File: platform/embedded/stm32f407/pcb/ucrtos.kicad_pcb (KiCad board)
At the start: 2 copper layers, 2 parts, among them J1 nes_gamepad_02x03, J2 STM32F4_Discovery_Header

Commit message: platform stm32f4: pcb: update pcb
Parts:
- moved J1 118.1 mm to (59.7, 120.7), turned to 270 degrees
- moved J2 12.5 mm to (94.4, 78.7)
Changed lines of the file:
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@@
   (general
     (thickness 1.6)
-    (drawings 0)
+    (drawings 2)
     (tracks 0)
     (zones 0)
@@
   )
   (module Connector_IDC:IDC-Header_2x03_P2.54mm_Vertical (layer F.Cu)
-    (at 160.02 58.42)
+    (at 59.69 120.65 270)
     (descr "Through hole straight IDC box header, 2x03, 2.54mm pitch, double rows")
     (tags "Through hole IDC box header THT 2x03 2.54mm double row")
-    (fp_text reference J1 (at 1.27 -6.604) (layer F.SilkS)
+    (fp_text reference J1 (at 1.27 -6.604 270) (layer F.SilkS)
       (effects (font (size 1 1) (thickness 0.15)))
     )
-    (fp_text value nes_gamepad_02x03 (at 1.27 11.684) (layer F.Fab)
+    (fp_text value nes_gamepad_02x03 (at 1.27 11.684 270) (layer F.Fab)
       (effects (font (size 1 1) (thickness 0.15)))
     )
-    (fp_text user %R (at 1.27 2.54) (layer F.Fab)
+    (fp_text user %R (at 1.27 2.54 270) (layer F.Fab)
       (effects (font (size 1 1) (thickness 0.15)))
     )
@@
     (fp_line (start -3.655 -5.6) (end -3.655 -3.06) (layer F.SilkS) (width 0.12))
     (fp_line (start -3.655 -5.6) (end -1.115 -5.6) (layer F.SilkS) (width 0.12))
-    (pad 1 thru_hole rect (at 0 0) (size 1.7272 1.7272) (drill 1.016) (layers *.Cu *.Mask))
-    (pad 2 thru_hole oval (at 2.54 0) (size 1.7272 1.7272) (drill 1.016) (layers *.Cu *.Mask))
-    (pad 3 thru_hole oval (at 0 2.54) (size 1.7272 1.7272) (drill 1.016) (layers *.Cu *.Mask))
-    (pad 4 thru_hole oval (at 2.54 2.54) (size 1.7272 1.7272) (drill 1.016) (layers *.Cu *.Mask))
-    (pad 5 thru_hole oval (at 0 5.08) (size 1.7272 1.7272) (drill 1.016) (layers *.Cu *.Mask))
-    (pad 6 thru_hole oval (at 2.54 5.08) (size 1.7272 1.7272) (drill 1.016) (layers *.Cu *.Mask))
+    (pad 1 thru_hole rect (at 0 0 270) (size 1.7272 1.7272) (drill 1.016) (layers *.Cu *.Mask))
+    (pad 2 thru_hole oval (at 2.54 0 270) (size 1.7272 1.7272) (drill 1.016) (layers *.Cu *.Mask))
+    (pad 3 thru_hole oval (at 0 2.54 270) (size 1.7272 1.7272) (drill 1.016) (layers *.Cu *.Mask))
+    (pad 4 thru_hole oval (at 2.54 2.54 270) (size 1.7272 1.7272) (drill 1.016) (layers *.Cu *.Mask))
+    (pad 5 thru_hole oval (at 0 5.08 270) (size 1.7272 1.7272) (drill 1.016) (layers *.Cu *.Mask))
+    (pad 6 thru_hole oval (at 2.54 5.08 270) (size 1.7272 1.7272) (drill 1.016) (layers *.Cu *.Mask))
     (model ${KISYS3DMOD}/Connector_IDC.3dshapes/IDC-Header_2x03_P2.54mm_Vertical.wrl
       (at (xyz 0 0 0))
@@
   )
   (module w_conn_misc:stm32f4_discovery_header (layer F.Cu)
-    (at 94.410501 66.210501)
+    (at 94.410501 78.74)
     (descr "STM32 F4 Discovery Header")
     (tags "STM32F4 Discovery")
@@
     )
   )
+  (dimension 100.33 (width 0.3) (layer F.SilkS)
+    (gr_text "100.330 mm" (at 95.885 135.45) (layer F.SilkS)
+      (effects (font (size 1.5 1.5) (thickness 0.3)))
+    )
+    (feature1 (pts (xy 146.05 101.6) (xy 146.05 133.936421)))
+    (feature2 (pts (xy 45.72 101.6) (xy 45.72 133.936421)))
+    (crossbar (pts (xy 45.72 133.35) (xy 146.05 133.35)))
+    (arrow1a (pts (xy 146.05 133.35) (xy 144.923496 133.936421)))
+    (arrow1b (pts (xy 146.05 133.35) (xy 144.923496 132.763579)))
+    (arrow2a (pts (xy 45.72 133.35) (xy 46.846504 133.936421)))
+    (arrow2b (pts (xy 45.72 133.35) (xy 46.846504 132.763579)))
+  )
+  (dimension 100.33 (width 0.3) (layer F.SilkS)
+    (gr_text "100.330 mm" (at 32.190001 83.185 270) (layer F.SilkS)
+      (effects (font (size 1.5 1.5) (thickness 0.3)))
+    )
+    (feature1 (pts (xy 39.37 133.35) (xy 33.70358 133.35)))
+    (feature2 (pts (xy 39.37 33.02) (xy 33.70358 33.02)))
+    (crossbar (pts (xy 34.290001 33.02) (xy 34.290001 133.35)))
+    (arrow1a (pts (xy 34.290001 133.35) (xy 33.70358 132.223496)))
+    (arrow1b (pts (xy 34.290001 133.35) (xy 34.876422 132.223496)))
+    (arrow2a (pts (xy 34.290001 33.02) (xy 33.70358 34.146504)))
+    (arrow2b (pts (xy 34.290001 33.02) (xy 34.876422 34.146504)))
+  )
 )

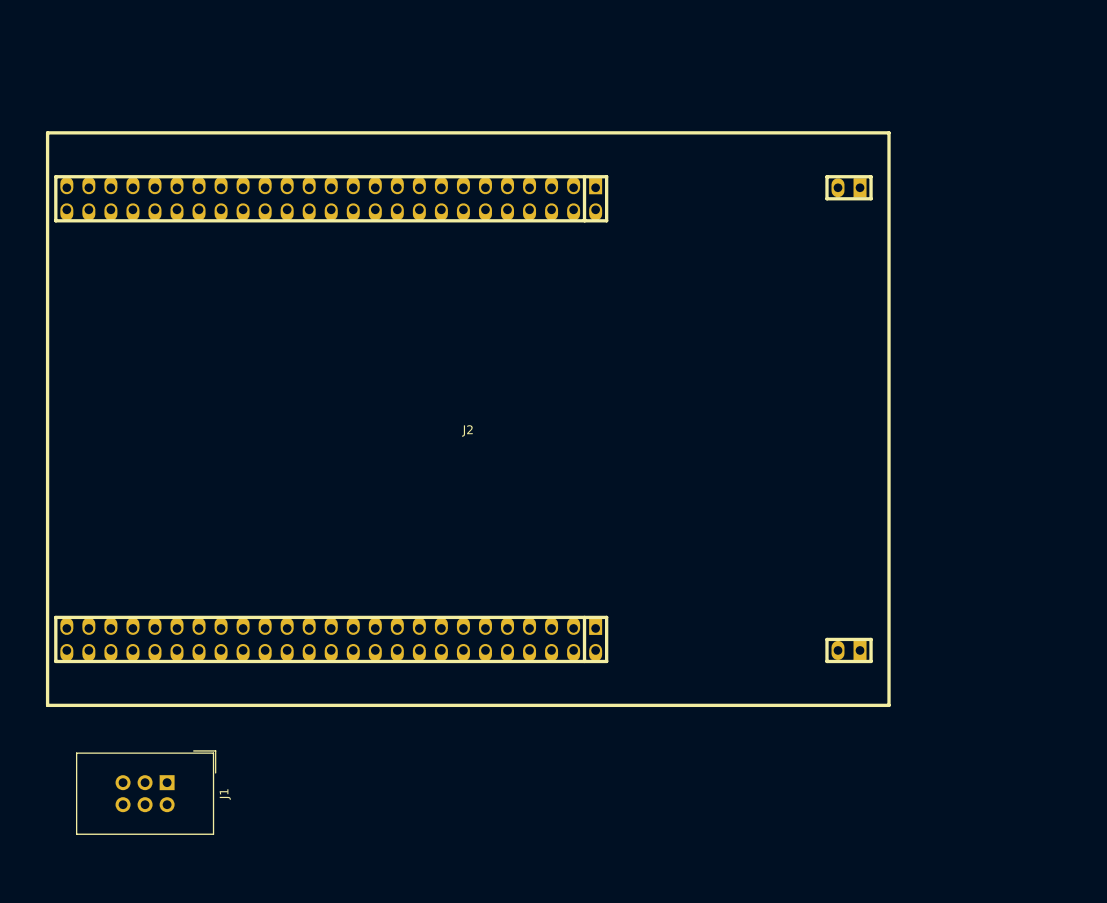
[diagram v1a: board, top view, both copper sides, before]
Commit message: platform stm32f4: pcb: place parts on pcb
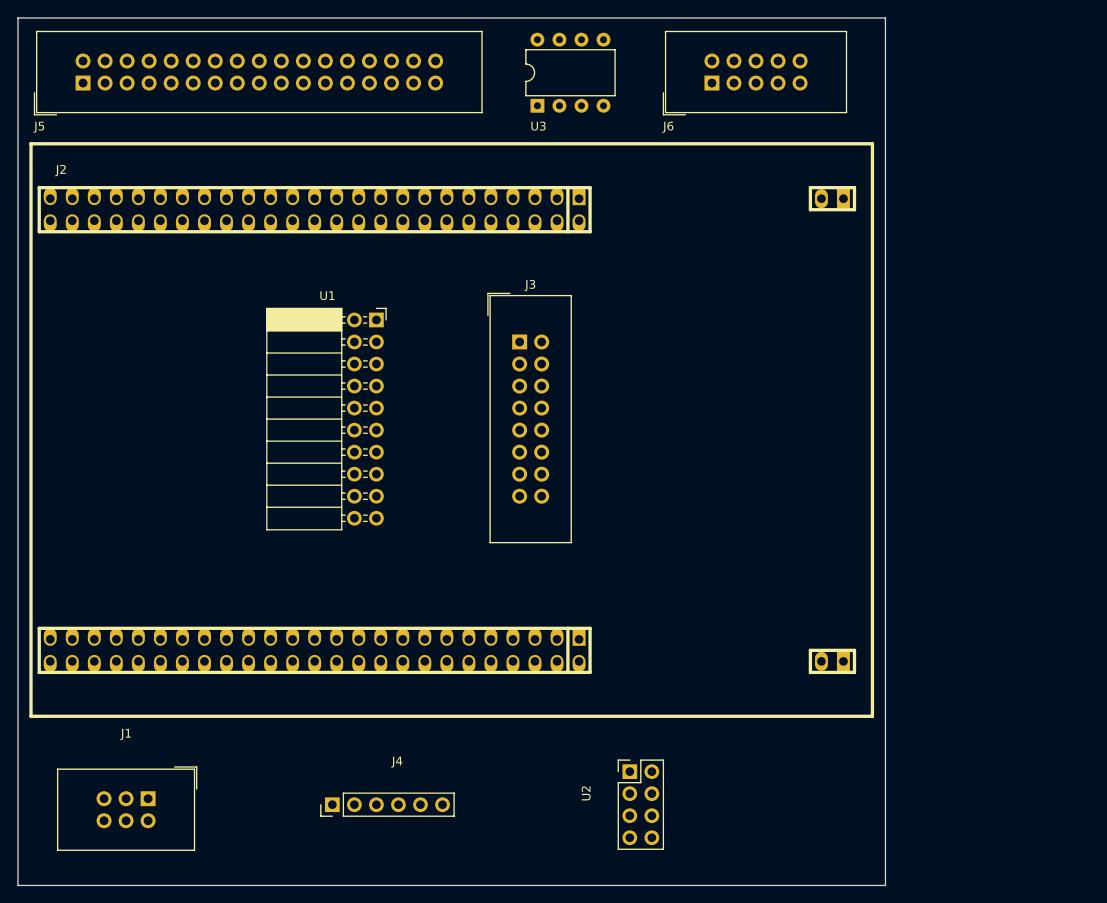
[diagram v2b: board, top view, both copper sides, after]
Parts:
- added J3: SD_Card, Connector_IDC:IDC-Header_2x08_P2.54mm_Vertical, F.Cu at (100.3, 69.8)
- added J4: FTDI, Connector_PinHeader_2.54mm:PinHeader_1x06_P2.54mm_Vertical, F.Cu at (78.7, 123.2)
- added J5: HY32D, Connector_IDC:IDC-Header_2x17_P2.54mm_Vertical, F.Cu at (50.0, 40.0)
- added J6: RS485, Connector_IDC:IDC-Header_2x05_P2.54mm_Vertical, F.Cu at (122.5, 40.0)
- added U1: DP83848_Breakout, Connector_PinSocket_2.54mm:PinSocket_2x10_P2.54mm_Horizontal, F.Cu at (83.8, 67.3)
- added U2: NRF24L01_Breakout, Connector_PinHeader_2.54mm:PinHeader_2x04_P2.54mm_Vertical, F.Cu at (113.0, 119.4)
- added U3: MAX485E, Package_DIP:DIP-8_W7.62mm, F.Cu at (102.4, 42.6)
- J1: value nes_gamepad_02x03 -> nes_gamepad
- moved J1 2.87 mm to (57.5, 122.5)
- moved J2 2.29 mm to (92.5, 80.0)
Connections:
- J1 pad 1: (no net) -> VCC
- J1 pad 2: (no net) -> /GAMEPAD_MISO
- J1 pad 3: (no net) -> Net-(J1-Pad3)
- J1 pad 4: (no net) -> /GAMEPAD_CS
- J1 pad 5: (no net) -> GND
- J1 pad 6: (no net) -> /GAMEPAD_SCK
- J2 pad 1: (no net) -> GND
- J2 pad 10: (no net) -> /GAMEPAD_MISO
- J2 pad 100: (no net) -> GND
- J2 pad 11: (no net) -> /ETH_OSCIN
- J2 pad 12: (no net) -> Net-(J2-Pad12)
- J2 pad 13: (no net) -> Net-(J2-Pad13)
- J2 pad 14: (no net) -> /ETH_MDIO
- J2 pad 15: (no net) -> Net-(J2-Pad15)
- J2 pad 16: (no net) -> Net-(J2-Pad16)
- J2 pad 17: (no net) -> /ETH_CRS_DV
- J2 pad 18: (no net) -> Net-(J2-Pad18)
- J2 pad 19: (no net) -> /ETH_RXD1
- J2 pad 2: (no net) -> GND
- J2 pad 20: (no net) -> /ETH_RXD0
- J2 pad 21: (no net) -> /RS485_DE
- J2 pad 22: (no net) -> /RS485_RE
- J2 pad 23: (no net) -> GND
- J2 pad 24: (no net) -> /GAMEPAD_CS
- J2 pad 25: (no net) -> /LCD_D4
- J2 pad 26: (no net) -> /LCD_D5
- J2 pad 27: (no net) -> /LCD_D6
- J2 pad 28: (no net) -> /LCD_D7
- J2 pad 29: (no net) -> /LCD_D8
- J2 pad 3: (no net) -> VCC
- J2 pad 30: (no net) -> /LCD_D9
- J2 pad 31: (no net) -> /LCD_D10
- J2 pad 32: (no net) -> /LCD_D11
- J2 pad 33: (no net) -> /LCD_D12
- J2 pad 34: (no net) -> /GAMEPAD_SCK
- J2 pad 35: (no net) -> /ETH_TX_EN
- J2 pad 36: (no net) -> /ETH_TXD0
- J2 pad 37: (no net) -> /ETH_TXD1
- J2 pad 38: (no net) -> Net-(J2-Pad38)
- J2 pad 39: (no net) -> Net-(J2-Pad39)
- J2 pad 4: (no net) -> VCC
- J2 pad 40: (no net) -> /LCD_D13
- J2 pad 41: (no net) -> /LCD_D14
- J2 pad 42: (no net) -> /LCD_D15
- J2 pad 43: (no net) -> /LCD_RS
- J2 pad 44: (no net) -> Net-(J2-Pad44)
- J2 pad 45: (no net) -> Net-(J2-Pad45)
- J2 pad 46: (no net) -> /LCD_D0
- J2 pad 47: (no net) -> /LCD_D1
- J2 pad 48: (no net) -> Net-(J2-Pad48)
- J2 pad 49: Net-(J2-Pad49) -> GND
- J2 pad 5: (no net) -> GND
- J2 pad 50: Net-(J2-Pad50) -> GND
- J2 pad 51: Net-(J2-Pad51) -> GND
- J2 pad 52: Net-(J2-Pad52) -> GND
- J2 pad 53: (no net) -> /RS485_DI
- J2 pad 54: (no net) -> /RS485_RO
- J2 pad 55: (no net) -> /SDIO_D0
- J2 pad 56: (no net) -> /SDIO_D1
- J2 pad 57: (no net) -> Net-(J2-Pad57)
- J2 pad 58: (no net) -> Net-(J2-Pad58)
- J2 pad 59: (no net) -> Net-(J2-Pad59)
- J2 pad 6: (no net) -> Net-(J2-Pad6)
- J2 pad 60: (no net) -> Net-(J2-Pad60)
- J2 pad 61: (no net) -> /LCD_BLCNT
- J2 pad 62: (no net) -> Net-(J2-Pad62)
- J2 pad 63: (no net) -> /SDIO_D2
- J2 pad 64: (no net) -> /SDIO_D3
- J2 pad 65: (no net) -> /SDIO_CK
- J2 pad 66: (no net) -> /LCD_D2
- J2 pad 67: (no net) -> /LCD_D3
- J2 pad 68: (no net) -> /SDIO_CMD
- J2 pad 69: (no net) -> Net-(J2-Pad69)
- J2 pad 7: (no net) -> /ETH_MDC
- J2 pad 70: (no net) -> /LCD_RD
- J2 pad 71: (no net) -> /LCD_WR
- J2 pad 72: (no net) -> Net-(J2-Pad72)
- J2 pad 73: (no net) -> /LCD_CS
- J2 pad 74: (no net) -> /NRF_SCK
- J2 pad 75: (no net) -> /NRF_MISO
- J2 pad 76: (no net) -> /NRF_MOSI
- J2 pad 77: (no net) -> /UART_DEBUG_TX
- J2 pad 78: (no net) -> /UART_DEBUG_RX
- J2 pad 79: (no net) -> Net-(J2-Pad79)
- J2 pad 8: (no net) -> /SDIO_CD
- J2 pad 80: (no net) -> VCC
- J2 pad 81: (no net) -> Net-(J2-Pad81)
- J2 pad 82: (no net) -> Net-(J2-Pad82)
- J2 pad 83: (no net) -> /LCD_RESET
- J2 pad 84: (no net) -> Net-(J2-Pad84)
- J2 pad 85: (no net) -> Net-(J2-Pad85)
- J2 pad 86: (no net) -> Net-(J2-Pad86)
- J2 pad 87: (no net) -> Net-(J2-Pad87)
- J2 pad 88: (no net) -> Net-(J2-Pad88)
- J2 pad 89: (no net) -> Net-(J2-Pad89)
- J2 pad 9: (no net) -> Net-(J2-Pad9)
- J2 pad 90: (no net) -> /NRF_CE
- J2 pad 91: (no net) -> /NRF_CSN
- J2 pad 92: (no net) -> /NRF_IRQ
- J2 pad 93: (no net) -> Net-(J2-Pad93)
- J2 pad 94: (no net) -> Net-(J2-Pad94)
- J2 pad 95: (no net) -> /STM32_3V3
- J2 pad 96: (no net) -> /STM32_3V3
- J2 pad 97: (no net) -> VCC
- J2 pad 98: (no net) -> VCC
- J2 pad 99: (no net) -> GND
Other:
- board outline added: 100 x 100 mm
